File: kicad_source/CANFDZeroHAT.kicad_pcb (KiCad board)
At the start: 2 copper layers, 65 x 30 mm, 31 parts, among them CN1 RASPI-IO, CN2 691322310004, CN3 GH_SM04B-GHS-TB, CN4 GH_SM04B-GHS-TB, SW1 JS202011JCQN, U1 MCP2518FD, U2 TCAN332GDR, Y1 RH100-20.000-20-3030-TR

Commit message: updated 40 MHz crystal
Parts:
- Y1: value RH100-20.000-20-3030-TR -> RH100-40.000-18-F-2050-TR

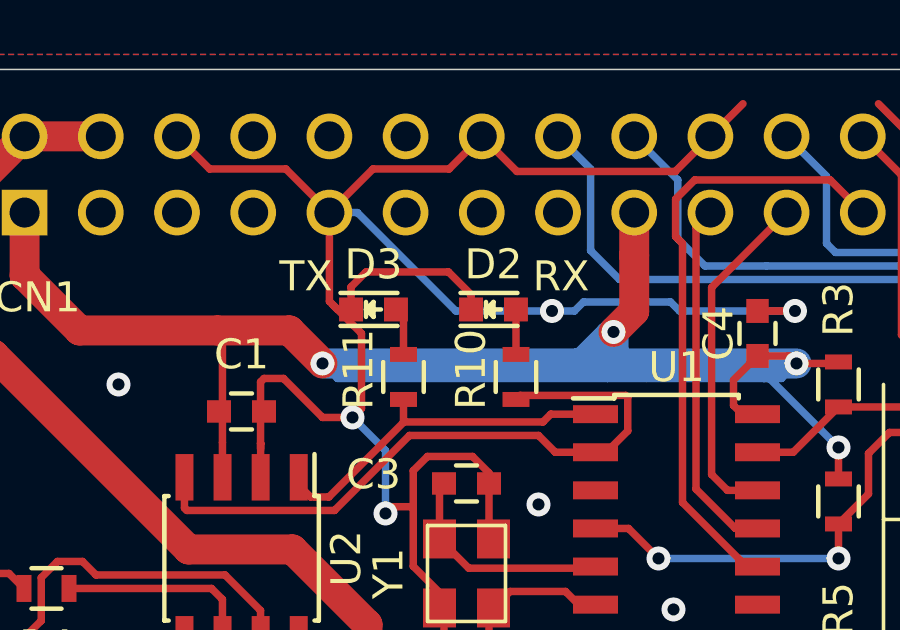
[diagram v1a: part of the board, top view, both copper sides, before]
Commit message: made debug leds low active
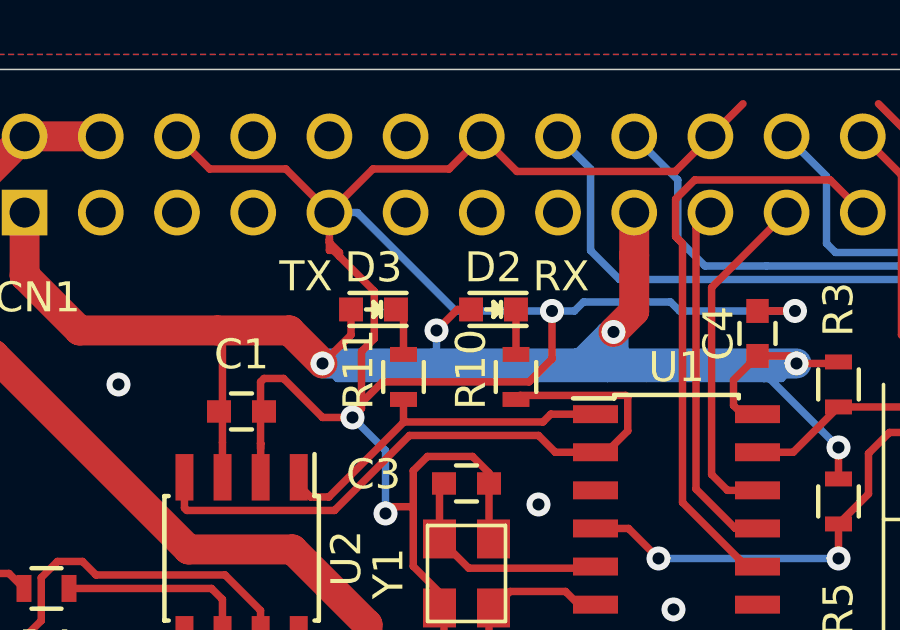
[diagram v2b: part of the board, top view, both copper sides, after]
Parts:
- turned D2 to 180 degrees
- turned D3 to 180 degrees
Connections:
- D2 pad 1: GND -> Net-(D2-Pad1)
- D2 pad 2: Net-(D2-Pad2) -> +3V3
- D3 pad 1: GND -> Net-(D3-Pad1)
- D3 pad 2: Net-(D3-Pad2) -> +3V3
- R10 pad 2: Net-(D2-Pad2) -> Net-(D2-Pad1)
- R11 pad 2: Net-(D3-Pad2) -> Net-(D3-Pad1)
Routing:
- net +3V3: track 68.3 -> 73.1 mm, vias 4 -> 5
- net GND: track 186.8 -> 190.6 mm
- net Net-(D3-Pad2): track 1.60 -> 0.00 mm
- net Net-(D3-Pad1): track 0.00 -> 1.60 mm
- net Net-(D2-Pad2): track 1.50 -> 0.00 mm
- net Net-(D2-Pad1): track 0.00 -> 1.50 mm

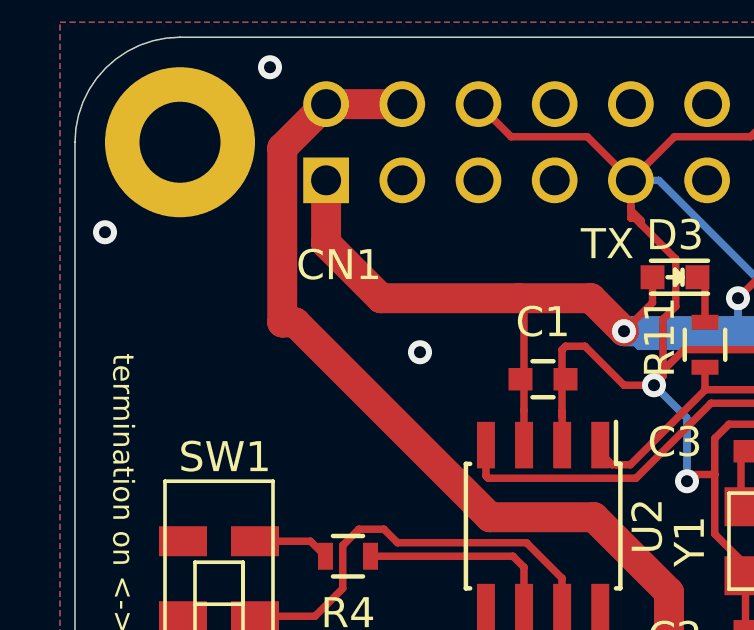
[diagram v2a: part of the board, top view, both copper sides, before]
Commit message: updated labels
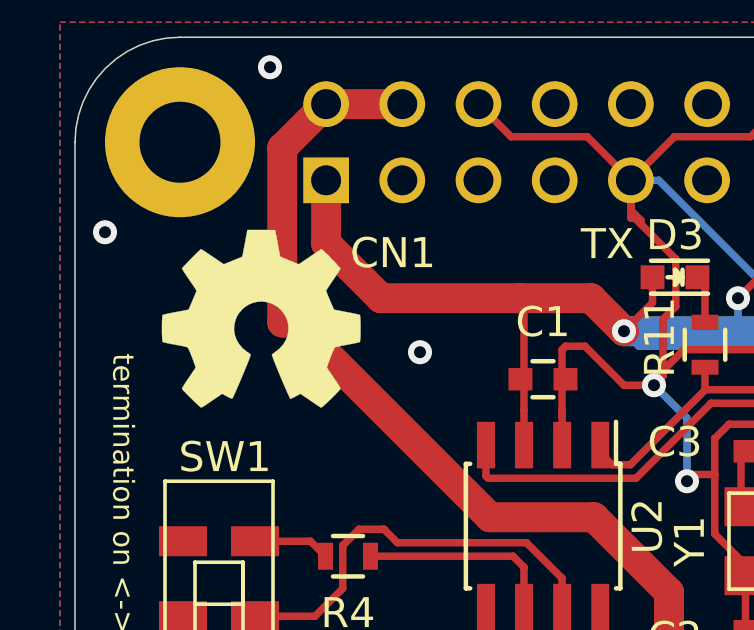
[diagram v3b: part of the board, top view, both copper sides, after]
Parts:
- added L3: Label, Symbol:OSHW-Symbol_6.7x6mm_SilkScreen, F.Cu at (113.7, 95.9)
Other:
- board text added: "Licensed under CERN OHL v.1.2"

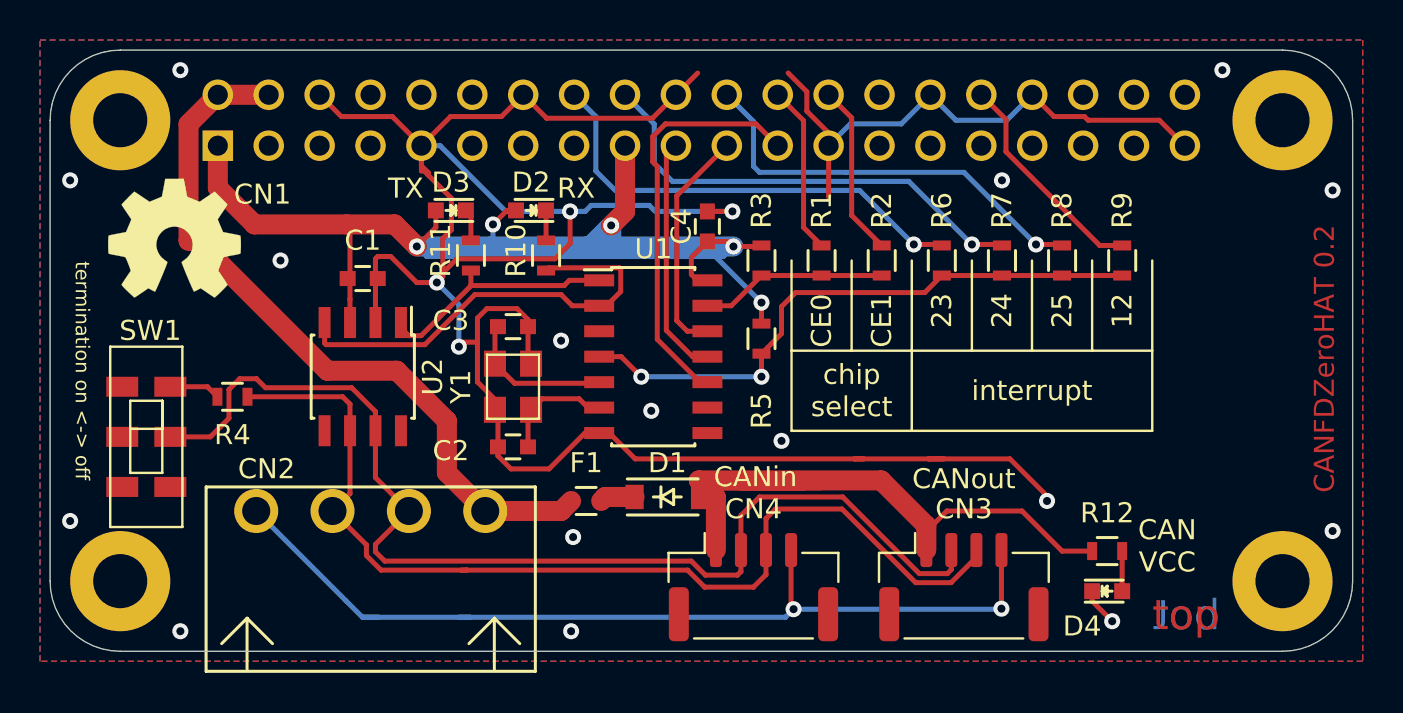
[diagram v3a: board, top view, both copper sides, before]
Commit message: updated project to KiCAD 6
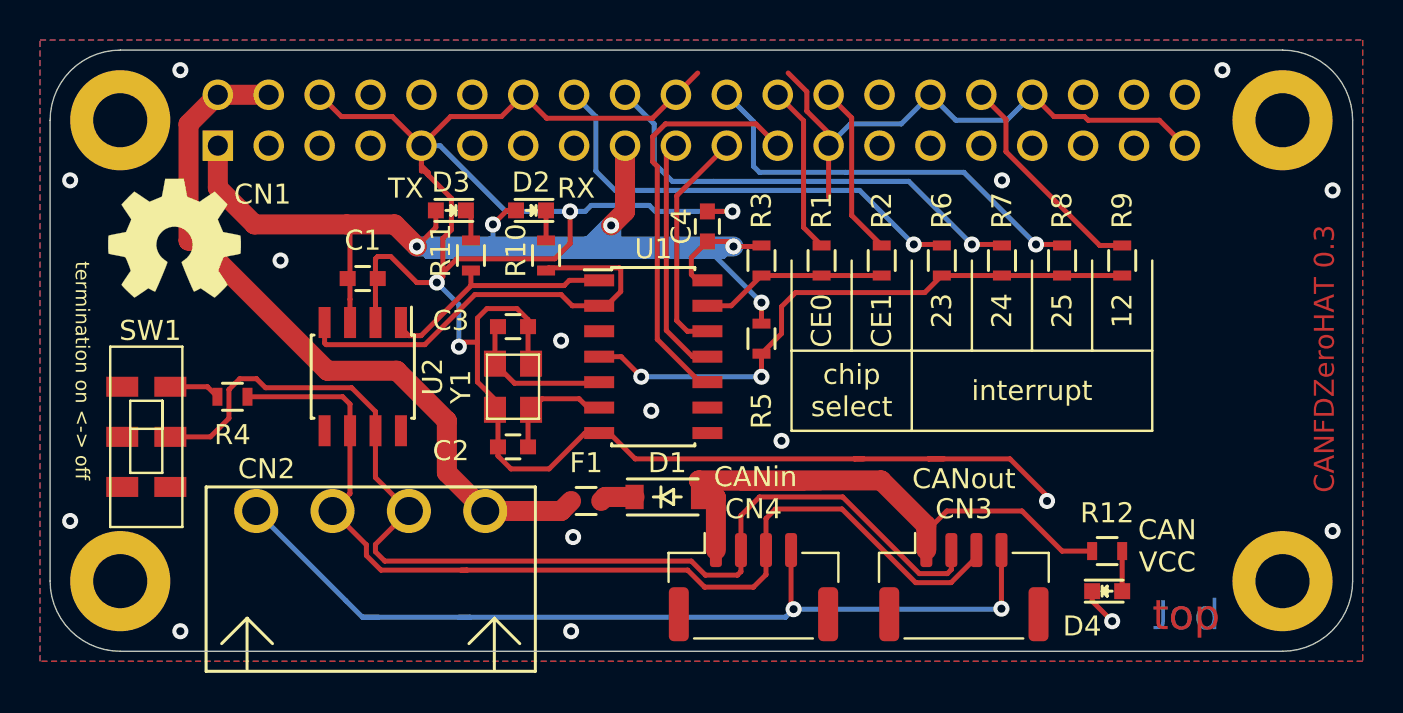
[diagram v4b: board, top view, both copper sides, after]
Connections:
- net +3V3 renamed +3.3V
- CN1 pad 10: (no net) -> /SERIAL_RX
- CN1 pad 11: (no net) -> unconnected-(CN1-Pad11)
- CN1 pad 12: (no net) -> unconnected-(CN1-Pad12)
- CN1 pad 13: (no net) -> unconnected-(CN1-Pad13)
- CN1 pad 15: (no net) -> unconnected-(CN1-Pad15)
- CN1 pad 27: (no net) -> unconnected-(CN1-Pad27)
- CN1 pad 28: (no net) -> unconnected-(CN1-Pad28)
- CN1 pad 29: (no net) -> unconnected-(CN1-Pad29)
- CN1 pad 3: (no net) -> /I2C_SDA
- CN1 pad 31: (no net) -> unconnected-(CN1-Pad31)
- CN1 pad 33: (no net) -> unconnected-(CN1-Pad33)
- CN1 pad 35: (no net) -> unconnected-(CN1-Pad35)
- CN1 pad 36: (no net) -> unconnected-(CN1-Pad36)
- CN1 pad 37: (no net) -> unconnected-(CN1-Pad37)
- CN1 pad 38: (no net) -> unconnected-(CN1-Pad38)
- CN1 pad 40: (no net) -> unconnected-(CN1-Pad40)
- CN1 pad 5: (no net) -> /I2C_SCL
- CN1 pad 7: (no net) -> unconnected-(CN1-Pad7)
- CN1 pad 8: (no net) -> /SERIAL_TX
- SW1 pad 3: (no net) -> unconnected-(SW1-Pad3)
- U1 pad 3: (no net) -> unconnected-(U1-Pad3)
- U1 pad 8: (no net) -> unconnected-(U1-Pad8)
- U1 pad 9: (no net) -> unconnected-(U1-Pad9)
- U2 pad 5: (no net) -> unconnected-(U2-Pad5)
- U2 pad 8: (no net) -> unconnected-(U2-Pad8)
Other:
- net class Default removed
- board text added: "CANFDZeroHAT 0.3"
- board text removed: "CANFDZeroHAT 0.2"

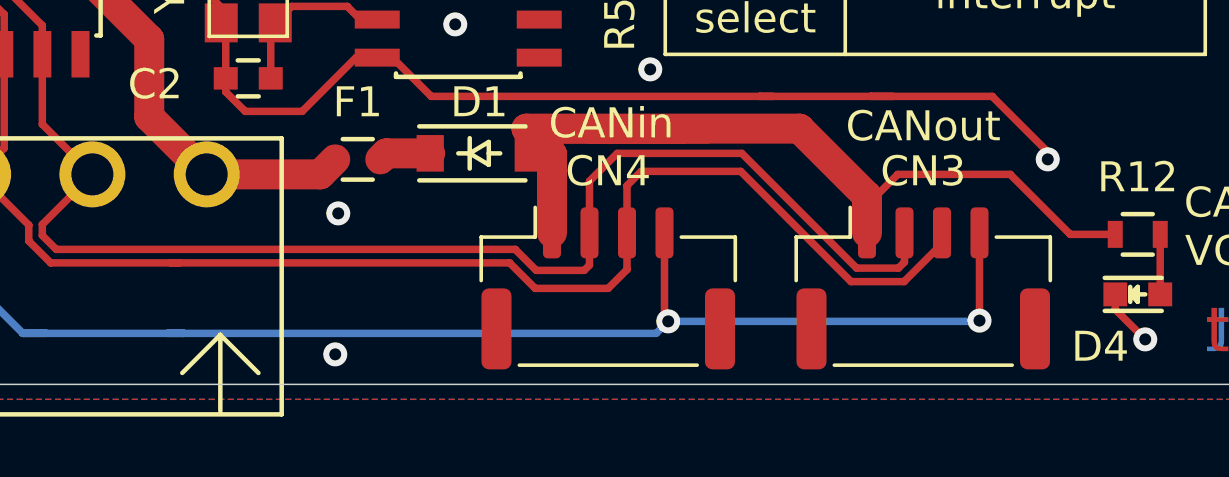
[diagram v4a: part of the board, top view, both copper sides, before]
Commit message: added mounting pad on CAN connector
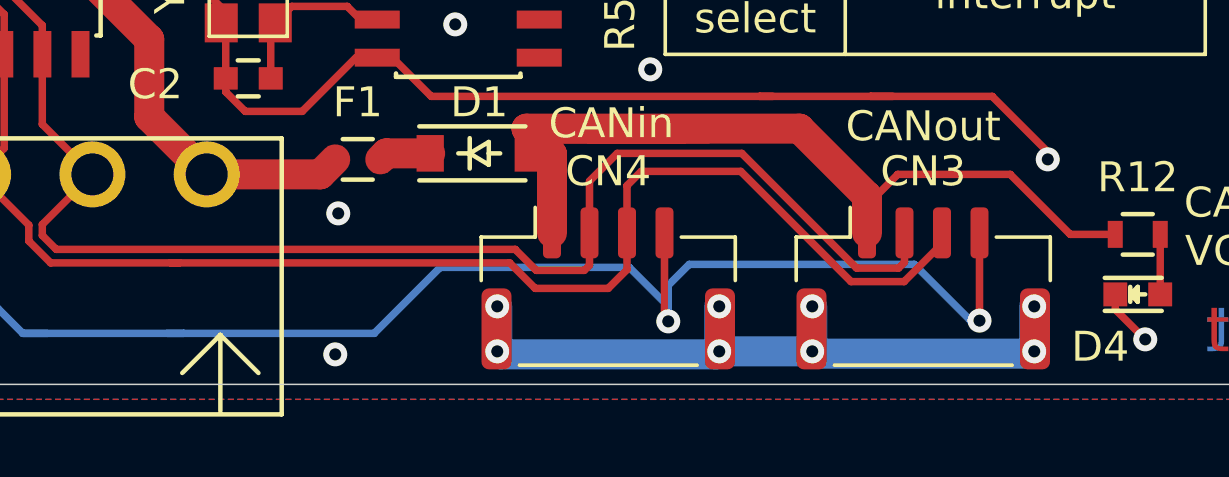
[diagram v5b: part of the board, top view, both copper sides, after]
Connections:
- CN3 pad MP: (no net) -> /MP
- CN4 pad MP: (no net) -> /MP
- SW1 pad 4: (no net) -> unconnected-(SW1-Pad4)
- SW1 pad 5: (no net) -> unconnected-(SW1-Pad5)
- SW1 pad 6: (no net) -> unconnected-(SW1-Pad6)
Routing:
- net /MP: track 0.00 -> 24.0 mm, vias 0 -> 8
- net GND: track 190.6 -> 194.7 mm

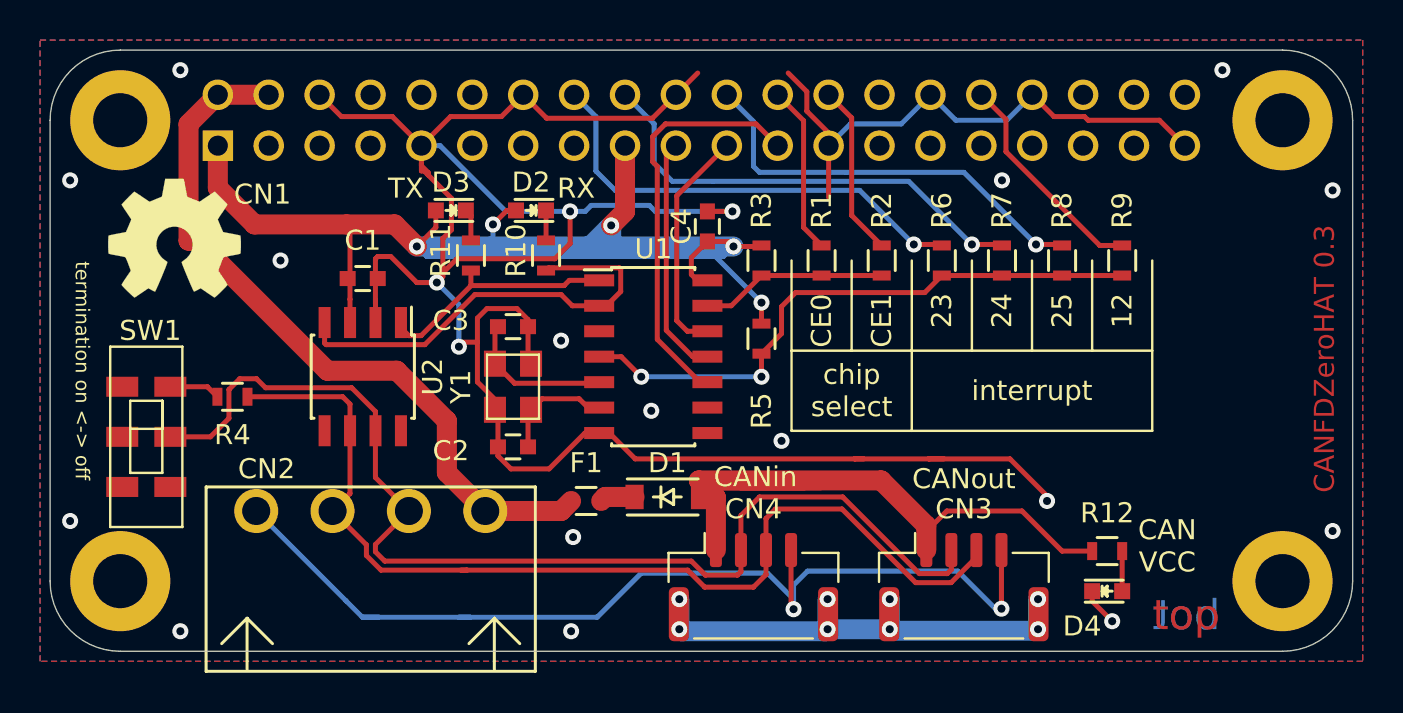
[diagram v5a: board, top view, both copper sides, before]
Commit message: updated footprints, added pulldown on SDO
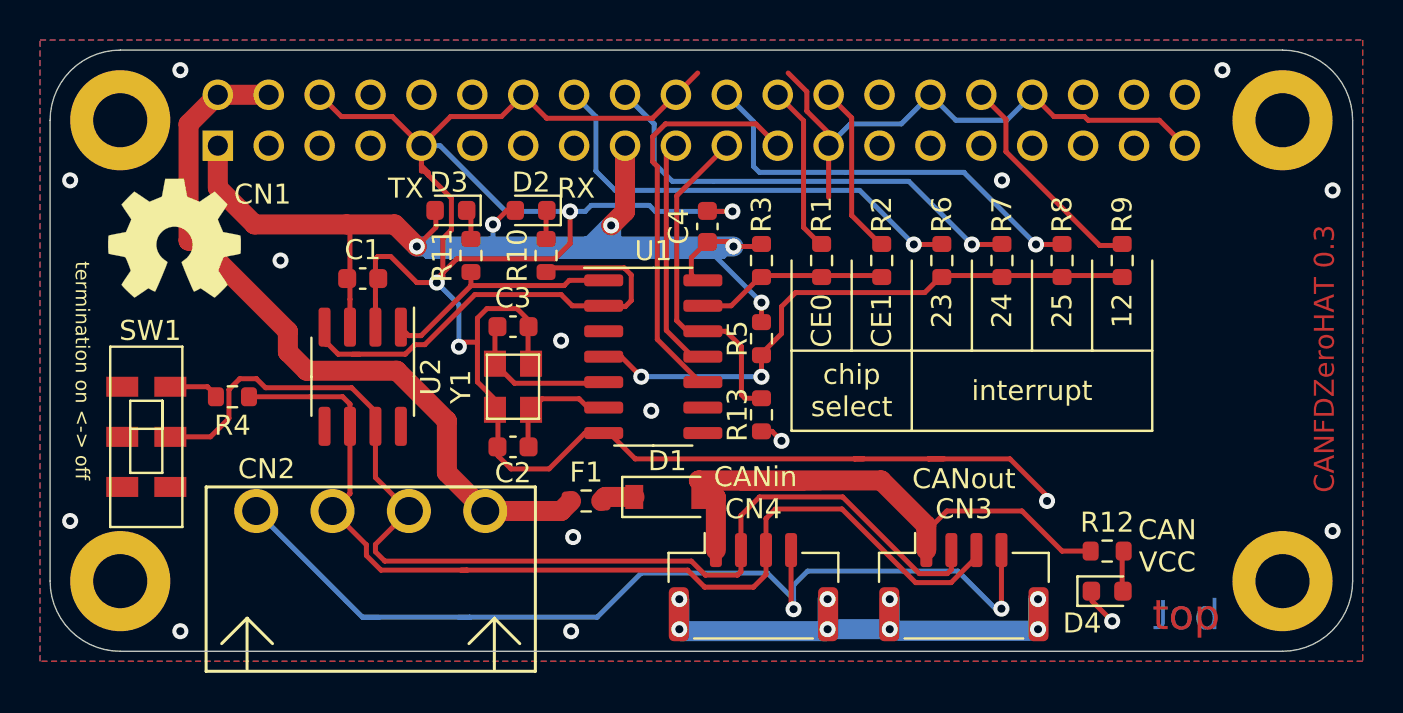
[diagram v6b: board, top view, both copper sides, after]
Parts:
- added R13: 10k, Resistor_SMD:R_0603_1608Metric, F.Cu at (143.0, 104.7)
- C1, C2, C3, C4: footprint capacitors:C_0603 -> Capacitor_SMD:C_0603_1608Metric
- D1: footprint diodes:SOD-123 -> Diode_SMD:D_SOD-123
- D2, D3, D4: footprint LEDs:LED_0603 -> LED_SMD:LED_0603_1608Metric
- F1, R1, R10, R11, R12, R2, R3, R4, R5, R6, R7, R8, R9: footprint resistors:R_0603 -> Resistor_SMD:R_0603_1608Metric
- U1: footprint SOIC:SOIC-14_3.9x8.7mm_Pitch1.27mm -> Package_SO:SOIC-14_3.9x8.7mm_P1.27mm
- U2: footprint SOIC:SOIC-8_3.9x4.9mm_Pitch1.27mm -> Package_SO:SOIC-8_3.9x4.9mm_P1.27mm
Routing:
- net /SPI_MISO: track 11.5 -> 17.2 mm
- net /CAN_RX: track 22.3 -> 25.2 mm
- net GND: track 194.7 -> 195.9 mm
- net +5V: track 36.8 -> 37.4 mm
